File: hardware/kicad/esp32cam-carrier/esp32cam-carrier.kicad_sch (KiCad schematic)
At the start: 14 parts, among them Q1 2N7000

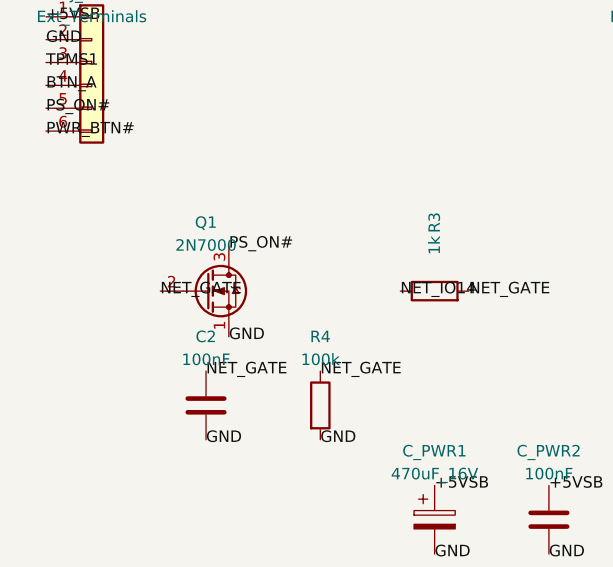
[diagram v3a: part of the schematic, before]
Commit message: feat(hardware): add esp32cam-carrier target and standardize bjt buffer
- Add [env:esp32cam-carrier] build environment with BOARD_ESP32CAM_CARRIER macro
- Standardize carrier PCB switch on BC547/BC548 NPN BJT (C-B-E pinout)
- Drive active-HIGH push-pull PS_ON# and read ADC2 oversampled hysteresis on carrier board
- Restore bare ESP32-CAM target to open-drain active-LOW and digital board sense
- Regenerate KiCad schematics, PCB, netlist, DRC report, BOM, and documentation
- Sync hardware-targets and power-control specs and archive change
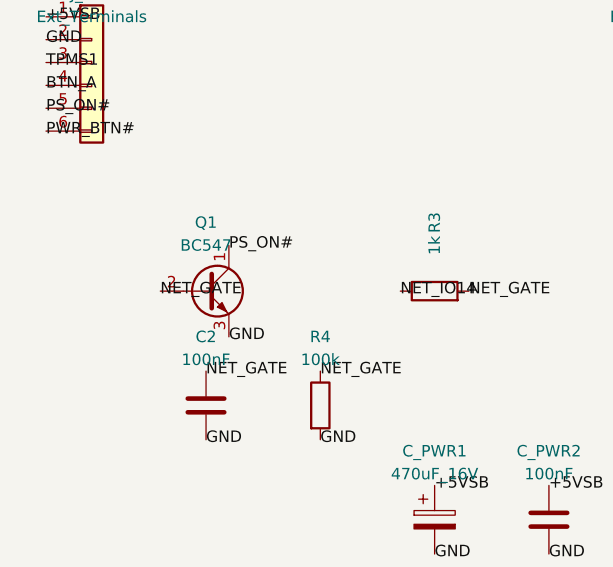
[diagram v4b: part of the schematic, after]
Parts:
- removed Q1: 2N7000, Package_TO_SOT_THT:TO-92_Inline_Wide, symbol Transistor_FET:2N7000
- added Q1: BC547, Package_TO_SOT_THT:TO-92_Inline, symbol Transistor_BJT:BC547
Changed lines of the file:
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@@
 	(title_block
 		(title "BC Awake ESP32-CAM Single-Layer Prototype Carrier Board")
-		(date "2026-10-20")
-		(rev "1.0")
+		(date "2026-10-22")
+		(rev "1.1")
 		(comment 1 "Single-layer PCB for protoboard replication")
-		(comment 2 "Bulk decoupling, TPMS1 RC filter, and PS_ON# MOSFET buffer")
+		(comment 2 "Bulk decoupling, TPMS1 RC filter, and PS_ON# BC547/BC548 NPN buffer")
 	)
 	(symbol
@@
 		(instances
 			(project "esp32cam-carrier"
-				(path "/f9fb3ae6-6c6b-44c8-a4d8-f85f21614183"
+				(path "/f42ac0a5-4d55-4092-b1ab-157e973d75e5"
 					(reference "J_EXT")
 					(unit 1)
@@
 		(instances
 			(project "esp32cam-carrier"
-				(path "/f9fb3ae6-6c6b-44c8-a4d8-f85f21614183"
+				(path "/f42ac0a5-4d55-4092-b1ab-157e973d75e5"
 					(reference "J_CAM_L")
 					(unit 1)
@@
 		(instances
 			(project "esp32cam-carrier"
-				(path "/f9fb3ae6-6c6b-44c8-a4d8-f85f21614183"
+				(path "/f42ac0a5-4d55-4092-b1ab-157e973d75e5"
 					(reference "J_CAM_R")
 					(unit 1)
@@
 		(instances
 			(project "esp32cam-carrier"
-				(path "/f9fb3ae6-6c6b-44c8-a4d8-f85f21614183"
+				(path "/f42ac0a5-4d55-4092-b1ab-157e973d75e5"
 					(reference "C_PWR1")
 					(unit 1)
@@
 		(instances
 			(project "esp32cam-carrier"
-				(path "/f9fb3ae6-6c6b-44c8-a4d8-f85f21614183"
+				(path "/f42ac0a5-4d55-4092-b1ab-157e973d75e5"
 					(reference "C_PWR2")
 					(unit 1)
@@
 		(instances
 			(project "esp32cam-carrier"
-				(path "/f9fb3ae6-6c6b-44c8-a4d8-f85f21614183"
+				(path "/f42ac0a5-4d55-4092-b1ab-157e973d75e5"
 					(reference "C_PWR3")
 					(unit 1)
@@
 		(instances
 			(project "esp32cam-carrier"
-				(path "/f9fb3ae6-6c6b-44c8-a4d8-f85f21614183"
+				(path "/f42ac0a5-4d55-4092-b1ab-157e973d75e5"
 					(reference "C_PWR4")
 					(unit 1)
@@
 		(instances
 			(project "esp32cam-carrier"
-				(path "/f9fb3ae6-6c6b-44c8-a4d8-f85f21614183"
+				(path "/f42ac0a5-4d55-4092-b1ab-157e973d75e5"
 					(reference "R1")
 					(unit 1)
@@
 		(instances
 			(project "esp32cam-carrier"
-				(path "/f9fb3ae6-6c6b-44c8-a4d8-f85f21614183"
+				(path "/f42ac0a5-4d55-4092-b1ab-157e973d75e5"
 					(reference "R2")
 					(unit 1)
@@
 		(instances
 			(project "esp32cam-carrier"
-				(path "/f9fb3ae6-6c6b-44c8-a4d8-f85f21614183"
+				(path "/f42ac0a5-4d55-4092-b1ab-157e973d75e5"
 					(reference "C1")
 					(unit 1)
@@
 	)
 	(symbol
-		(lib_id "Transistor_FET:2N7000")
+		(lib_id "Transistor_BJT:BC547")
 		(at 63.5 88.9 0)
 		(unit 1)
@@
 			(effects (font (size 1.27 1.27)))
 		)
-		(property "Value" "2N7000"
+		(property "Value" "BC547"
 			(at 63.5 83.82000000000001 0)
 			(effects (font (size 1.27 1.27)))
 		)
-		(property "Footprint" "Package_TO_SOT_THT:TO-92_Inline_Wide"
+		(property "Footprint" "Package_TO_SOT_THT:TO-92_Inline"
 			(at 63.5 88.9 0)
 			(effects (font (size 1.27 1.27)) (hide yes))
@@
 			(effects (font (size 1.27 1.27)) (hide yes))
 		)
-		(property "Description" "PS_ON# Buffer"
+		(property "Description" "PS_ON# NPN Buffer"
 			(at 63.5 88.9 0)
 			(effects (font (size 1.27 1.27)) (hide yes))
@@
 		(instances
 			(project "esp32cam-carrier"
-				(path "/f9fb3ae6-6c6b-44c8-a4d8-f85f21614183"
+				(path "/f42ac0a5-4d55-4092-b1ab-157e973d75e5"
 					(reference "Q1")
 					(unit 1)
@@
 			(effects (font (size 1.27 1.27)) (hide yes))
 		)
-		(property "Description" "2N7000 gate resistor"
+		(property "Description" "BC547 base resistor"
 			(at 88.9 88.9 0)
 			(effects (font (size 1.27 1.27)) (hide yes))
@@
 		(instances
 			(project "esp32cam-carrier"
-				(path "/f9fb3ae6-6c6b-44c8-a4d8-f85f21614183"
+				(path "/f42ac0a5-4d55-4092-b1ab-157e973d75e5"
 					(reference "R3")
 					(unit 1)
@@
 			(effects (font (size 1.27 1.27)) (hide yes))
 		)
-		(property "Description" "2N7000 gate pull-down"
+		(property "Description" "BC547 base pull-down"
 			(at 76.2 101.6 0)
 			(effects (font (size 1.27 1.27)) (hide yes))
@@
 		(instances
 			(project "esp32cam-carrier"
-				(path "/f9fb3ae6-6c6b-44c8-a4d8-f85f21614183"
+				(path "/f42ac0a5-4d55-4092-b1ab-157e973d75e5"
 					(reference "R4")
 					(unit 1)
@@
 			(effects (font (size 1.27 1.27)) (hide yes))
 		)
-		(property "Description" "2N7000 gate snubber"
+		(property "Description" "BC547 base snubber"
 			(at 63.5 101.6 0)
 			(effects (font (size 1.27 1.27)) (hide yes))
@@
 		(instances
 			(project "esp32cam-carrier"
-				(path "/f9fb3ae6-6c6b-44c8-a4d8-f85f21614183"
+				(path "/f42ac0a5-4d55-4092-b1ab-157e973d75e5"
 					(reference "C2")
 					(unit 1)
@@
 	(label "GND" (at 101.6 34.29 0) (effects (font (size 1.27 1.27))))
 	(label "NET_IO13" (at 101.6 41.91 0) (effects (font (size 1.27 1.27))))
+	(label "PS_ON#" (at 66.04 83.82 0) (effects (font (size 1.27 1.27))))
+	(label "NET_GATE" (at 58.42 88.9 0) (effects (font (size 1.27 1.27))))
 	(label "GND" (at 66.04 93.98 0) (effects (font (size 1.27 1.27))))
-	(label "NET_GATE" (at 58.42 88.9 0) (effects (font (size 1.27 1.27))))
-	(label "PS_ON#" (at 66.04 83.82 0) (effects (font (size 1.27 1.27))))
 	(label "NET_IO14" (at 85.09 88.9 0) (effects (font (size 1.27 1.27))))
 	(label "NET_GATE" (at 92.71 88.9 0) (effects (font (size 1.27 1.27))))
@@
 	(label "GND" (at 63.5 105.41 0) (effects (font (size 1.27 1.27))))
 	(sheet_instances
-		(path "/f9fb3ae6-6c6b-44c8-a4d8-f85f21614183"
+		(path "/f42ac0a5-4d55-4092-b1ab-157e973d75e5"
 			(page "1")
 		)
